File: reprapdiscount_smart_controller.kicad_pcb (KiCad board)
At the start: 2 copper layers, 150 x 55 mm, 17 parts, among them Q1 BC817, U1 74HC4050, U2 MIC5209

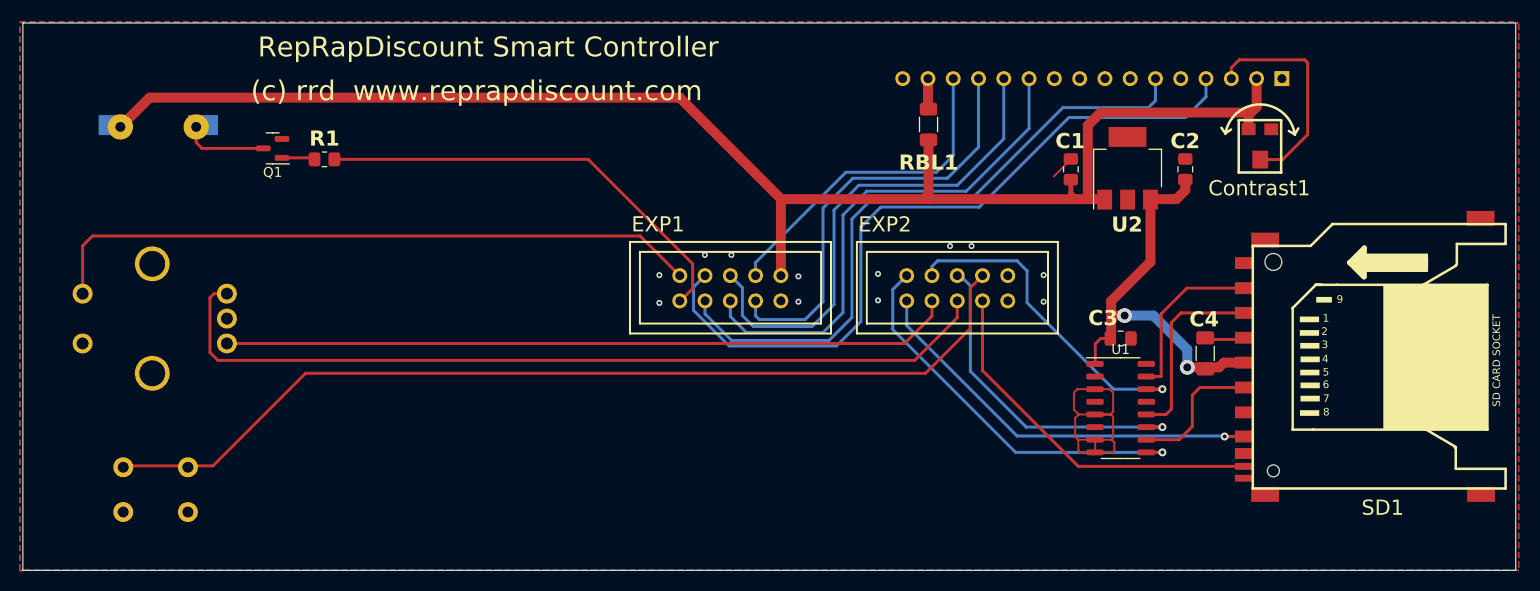
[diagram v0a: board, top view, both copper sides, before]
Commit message: fixup: restore mounting holes lost during cleanup
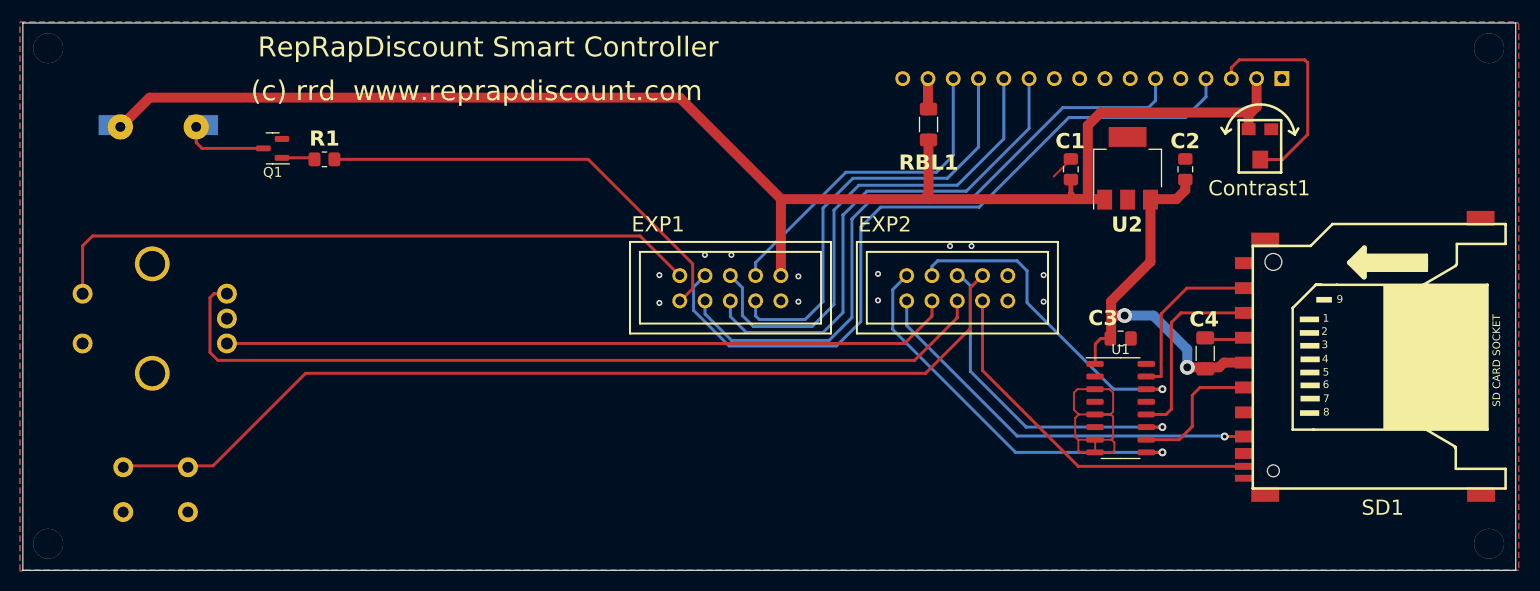
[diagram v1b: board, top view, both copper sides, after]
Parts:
- added H1: MountingHole, reprapdiscount_smart_controller:MountingHole_3mm, F.Cu at (76.0, 80.0)
- added H2: MountingHole, reprapdiscount_smart_controller:MountingHole_3mm, F.Cu at (220.8, 80.0)
- added H3: MountingHole, reprapdiscount_smart_controller:MountingHole_3mm, F.Cu at (76.0, 129.8)
- added H4: MountingHole, reprapdiscount_smart_controller:MountingHole_3mm, F.Cu at (220.8, 129.8)

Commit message: fixup: fix reset button height
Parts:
- PB1: footprint Button_Switch_THT:SW_PUSH_6mm_H5mm -> Button_Switch_THT:SW_PUSH_6mm_H7.3mm
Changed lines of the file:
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@@
     )
   )
-  (footprint "Button_Switch_THT:SW_PUSH_6mm_H5mm" locked (layer "B.Cu")
+  (footprint "Button_Switch_THT:SW_PUSH_6mm_H7.3mm" locked (layer "B.Cu")
     (at 90.0841 122.1436 180)
-    (descr "tactile push button, 6x6mm e.g. PHAP33xx series, height=5mm")
+    (descr "tactile push button, 6x6mm e.g. PHAP33xx series, height=7.3mm")
     (tags "tact sw push 6mm")
     (property "Sheetfile" "reprapdiscount_smart_controller.kicad_sch")
@@
     (property "ki_keywords" "switch normally-open pushbutton push-button")
     (attr through_hole)
-    (fp_text reference "PB1" (at 3.25 2.286) (layer "B.SilkS")
-        (effects (font (size 1.524 1.524) (thickness 0.254) bold) (justify mirror))
+    (fp_text reference "PB1" (at 3.25 2) (layer "B.SilkS")
+        (effects (font (size 1 1) (thickness 0.15)) (justify mirror))
     )
-    (fp_text value "STOP" (at 3.75 -6.985) (layer "B.SilkS")
-        (effects (font (size 1.524 1.524) (thickness 0.254) bold) (justify mirror))
+    (fp_text value "STOP" (at 3.75 -6.7) (layer "B.Fab")
+        (effects (font (size 1 1) (thickness 0.15)) (justify mirror))
     )
     (fp_text user "${REFERENCE}" (at 3.25 -2.25) (layer "B.Fab")
@@
     (pad "2" thru_hole circle locked (at 6.5 -4.5 90) (size 2 2) (drill 1.1) (layers "*.Cu" "*.Mask")
       (net 6 "GND") (pinfunction "2") (pintype "passive"))
-    (model "${KICAD6_3DMODEL_DIR}/Button_Switch_THT.3dshapes/SW_PUSH_6mm_H5mm.wrl"
+    (model "${KICAD6_3DMODEL_DIR}/Button_Switch_THT.3dshapes/SW_PUSH_6mm_H7.3mm.wrl"
       (offset (xyz 0 0 0))
       (scale (xyz 1 1 1))

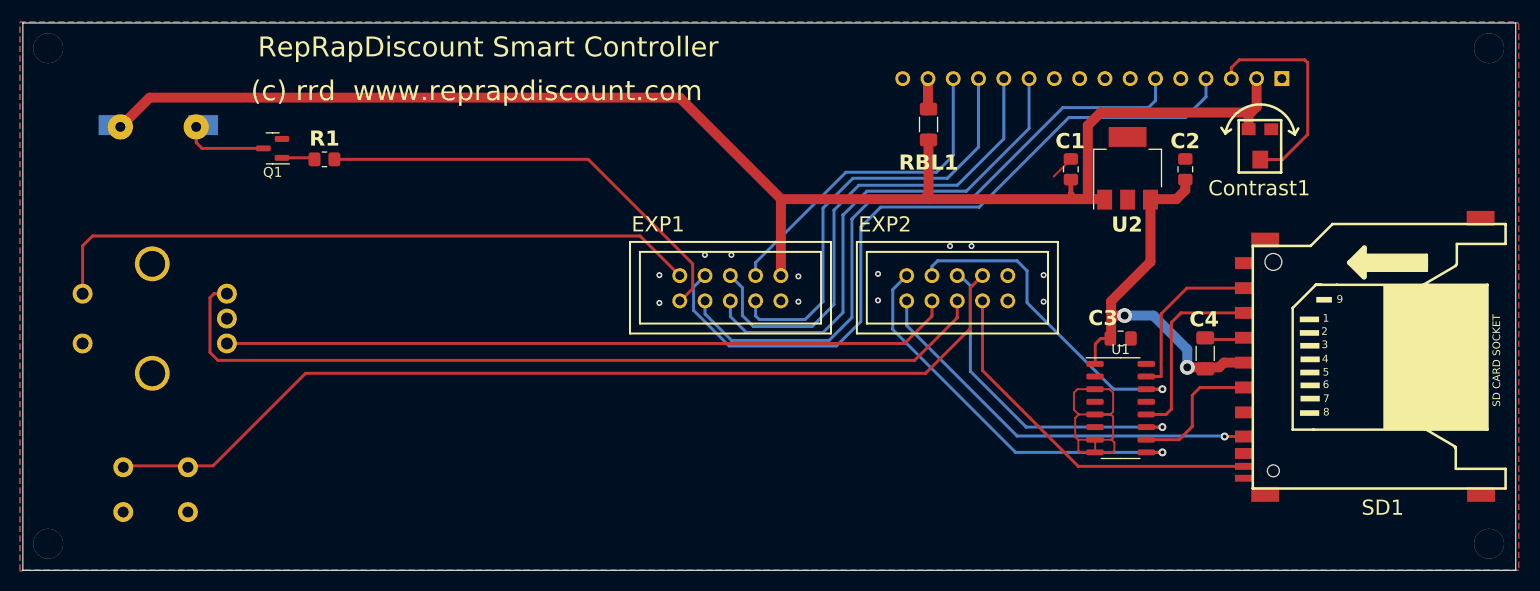
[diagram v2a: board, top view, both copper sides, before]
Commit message: feature: add parts from ldo-rrlcd-a007
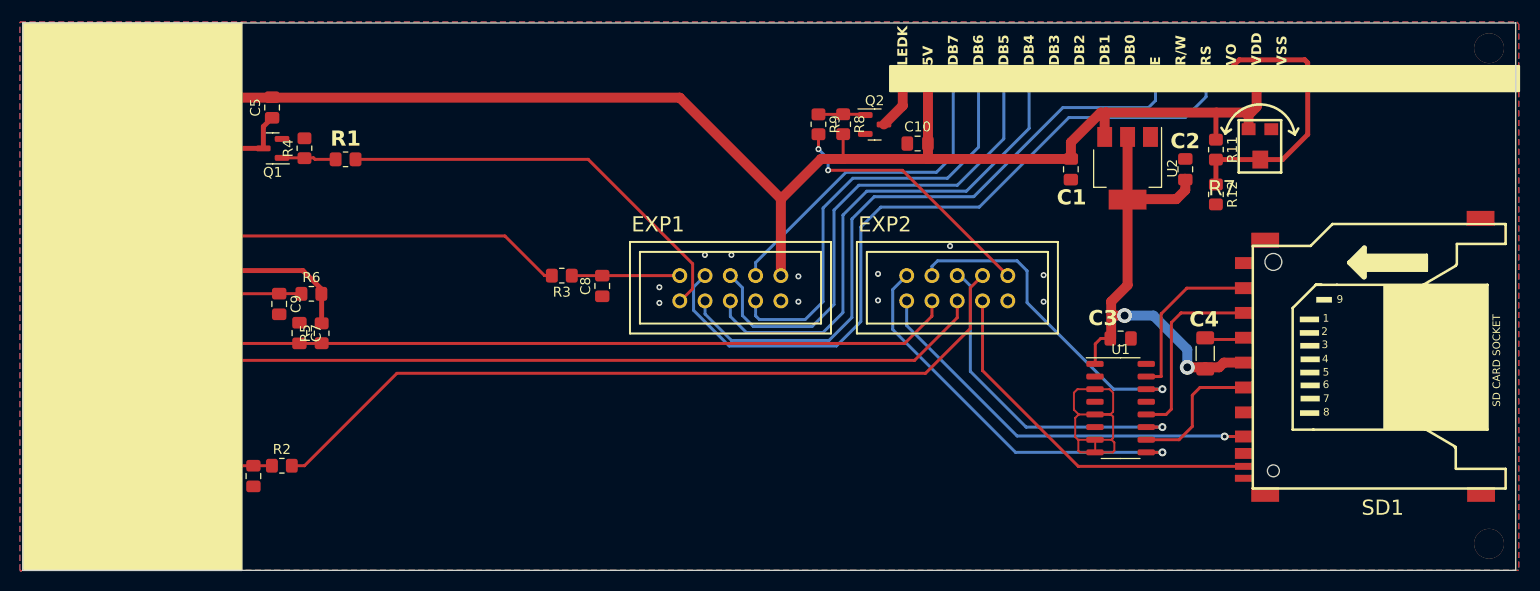
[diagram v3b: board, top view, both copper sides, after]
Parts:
- removed RBL1: 68, Resistor_SMD:R_1206_3216Metric_Pad1.30x1.75mm_HandSolder
- added C10: 10u, Capacitor_SMD:C_0805_2012Metric_Pad1.18x1.45mm_HandSolder, F.Cu at (163.4, 89.6)
- added C5: 100n, Capacitor_SMD:C_0805_2012Metric_Pad1.18x1.45mm_HandSolder, F.Cu at (98.5, 86.0)
- added C6: 100n, Capacitor_SMD:C_0805_2012Metric_Pad1.18x1.45mm_HandSolder, F.Cu at (96.7, 123.0)
- added C7: 100n, Capacitor_SMD:C_0805_2012Metric_Pad1.18x1.45mm_HandSolder, F.Cu at (101.3, 108.7)
- added C8: 100n, Capacitor_SMD:C_0805_2012Metric_Pad1.18x1.45mm_HandSolder, F.Cu at (131.7, 103.9)
- added C9: 100n, Capacitor_SMD:C_0805_2012Metric_Pad1.18x1.45mm_HandSolder, F.Cu at (99.3, 105.7)
- added Q2: BC817, Package_TO_SOT_SMD:SOT-23, F.Cu at (159.1, 87.7)
- added R11: DNI, Resistor_SMD:R_0805_2012Metric_Pad1.20x1.40mm_HandSolder, F.Cu at (193.4, 90.2)
- added R12: 470R, Resistor_SMD:R_0805_2012Metric_Pad1.20x1.40mm_HandSolder, F.Cu at (193.4, 94.7)
- added R2: 1k, Resistor_SMD:R_0805_2012Metric_Pad1.20x1.40mm_HandSolder, F.Cu at (99.5, 122.0)
- added R3: 100R, Resistor_SMD:R_0805_2012Metric_Pad1.20x1.40mm_HandSolder, F.Cu at (127.7, 102.9)
- added R4: 5.1k, Resistor_SMD:R_0805_2012Metric_Pad1.20x1.40mm_HandSolder, F.Cu at (101.8, 90.1)
- added R5: 5.1k, Resistor_SMD:R_0805_2012Metric_Pad1.20x1.40mm_HandSolder, F.Cu at (103.5, 108.7)
- added R6: 5.1k, Resistor_SMD:R_0805_2012Metric_Pad1.20x1.40mm_HandSolder, F.Cu at (102.5, 104.7)
- added R8: 10k, Resistor_SMD:R_0805_2012Metric_Pad1.20x1.40mm_HandSolder, F.Cu at (155.9, 87.7)
- added R9: 100R, Resistor_SMD:R_0805_2012Metric_Pad1.20x1.40mm_HandSolder, F.Cu at (153.4, 87.7)
- C1, C2: value 100nF -> 10u
- C3: value 100nF -> 100n
- C4: value 1uF -> 10u
- R7: renamed from Contrast1; value 10K -> 1.4k
- U2: value MIC5209 -> AMS1117-3.3; footprint Package_TO_SOT_SMD:SOT-223 -> Package_TO_SOT_SMD:SOT-223-3_TabPin2
- moved R1 2.12 mm to (105.9, 91.2)
- turned C1 to 90 degrees
- turned U2 to -90 degrees
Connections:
- EN1 pad 5: BTN_ENC -> Net-(EN1-Pad5)
- EXP2 pad 10: /KILL -> PWR_LED
- LCD1 pad 15: Net-(LCD1-A+) -> VCC
- LCD1 pad 16: GND -> LEDK
- PB1 pad 1: /RESET -> Net-(C6-Pad2)
- U2 pad 1: VCC -> GND
- U2 pad 2: GND -> +3V3
- U2 pad 3: +3V3 -> VCC
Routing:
- net BTN_ENC: track 66.9 -> 10.9 mm
- net VCC: track 150.3 -> 205.1 mm
- net Net-(EN1-Pad5): track 0.00 -> 51.2 mm
- net PWR_LED: track 0.00 -> 26.5 mm, vias 0 -> 2
- net /RESET: track 96.8 -> 79.7 mm
- net Net-(C6-Pad2): track 0.00 -> 17.0 mm
- net +3V3: track 41.2 -> 48.8 mm
- net BTN_EN1: track 86.2 -> 93.7 mm
- net Net-(LCD1-Vo): track 22.2 -> 29.2 mm
- net LEDK: track 0.00 -> 5.39 mm
- net Net-(Q2-B): track 0.00 -> 4.74 mm
- net Net-(PZ1-+): track 8.50 -> 11.9 mm
- net Net-(LCD1-A+): track 3.27 -> 0.00 mm
- net GND: track 36.3 -> 33.9 mm, vias 12 -> 11
- net BEEPER: track 44.6 -> 42.5 mm
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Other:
- board text added: "5V"
- board text added: "DB0"
- board text added: "DB1"
- board text added: "DB2"
- board text added: "DB3"
- board text added: "DB4"
- board text added: "DB5"
- board text added: "DB6"
- board text added: "DB7"
- board text added: "E"
- board text added: "LEDK"
- board text added: "R/W"
- board text added: "RS"
- board text added: "VO"
- board text added: "VSS"
- board text removed: "(c) rrd www.reprapdiscount.com"
- board text removed: "RepRapDiscount Smart Controller"

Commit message: feature: add fiducials
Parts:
- added FID1: Fiducial, Fiducial:Fiducial_1mm_Mask2mm, F.Cu at (103.5, 81.5)
- added FID2: Fiducial, Fiducial:Fiducial_1mm_Mask2mm, F.Cu at (213.5, 128.5)
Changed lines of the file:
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@@
     )
+  )
+  (footprint "Fiducial:Fiducial_1mm_Mask2mm" (layer "F.Cu")
+    (at 213.5011 128.5036)
+    (descr "Circular Fiducial, 1mm bare copper, 2mm soldermask opening (Level A)")
+    (tags "fiducial")
+    (property "Sheetfile" "reprapdiscount_smart_controller.kicad_sch")
+    (property "Sheetname" "")
+    (property "ki_description" "Fiducial Marker")
+    (property "ki_keywords" "fiducial marker")
+    (attr smd)
+    (fp_text reference "FID2" (at 0 -2) (layer "F.Fab")
+        (effects (font (size 1 1) (thickness 0.15)))
+    )
+    (fp_text value "Fiducial" (at 0 2) (layer "F.Fab")
+        (effects (font (size 1 1) (thickness 0.15)))
+    )
+    (fp_text user "${REFERENCE}" (at 0 0) (layer "F.Fab")
+        (effects (font (size 0.4 0.4) (thickness 0.06)))
+    )
+    (fp_circle (center 0 0) (end 1.25 0)
+      (stroke (width 0.05) (type solid)) (fill none) (layer "F.CrtYd"))
+    (fp_circle (center 0 0) (end 1 0)
+      (stroke (width 0.1) (type solid)) (fill none) (layer "F.Fab"))
+    (pad "" smd circle (at 0 0) (size 1 1) (layers "F.Cu" "F.Mask")
+      (solder_mask_margin 0.5) (clearance 0.5))
   )
   (footprint "Resistor_SMD:R_0805_2012Metric_Pad1.20x1.40mm_HandSolder" (layer "F.Cu")
@@
     )
   )
+  (footprint "Fiducial:Fiducial_1mm_Mask2mm" (layer "F.Cu")
+    (at 103.5011 81.5036)
+    (descr "Circular Fiducial, 1mm bare copper, 2mm soldermask opening (Level A)")
+    (tags "fiducial")
+    (property "Sheetfile" "reprapdiscount_smart_controller.kicad_sch")
+    (property "Sheetname" "")
+    (property "ki_description" "Fiducial Marker")
+    (property "ki_keywords" "fiducial marker")
+    (attr smd)
+    (fp_text reference "FID1" (at 0 -2) (layer "F.Fab")
+        (effects (font (size 1 1) (thickness 0.15)))
+    )
+    (fp_text value "Fiducial" (at 0 2) (layer "F.Fab")
+        (effects (font (size 1 1) (thickness 0.15)))
+    )
+    (fp_text user "${REFERENCE}" (at 0 0) (layer "F.Fab")
+        (effects (font (size 0.4 0.4) (thickness 0.06)))
+    )
+    (fp_circle (center 0 0) (end 1.25 0)
+      (stroke (width 0.05) (type solid)) (fill none) (layer "F.CrtYd"))
+    (fp_circle (center 0 0) (end 1 0)
+      (stroke (width 0.1) (type solid)) (fill none) (layer "F.Fab"))
+    (pad "" smd circle (at 0 0) (size 1 1) (layers "F.Cu" "F.Mask")
+      (solder_mask_margin 0.5) (clearance 0.5))
+  )
   (footprint "Button_Switch_THT:SW_PUSH_6mm_H7.3mm" locked (layer "B.Cu")

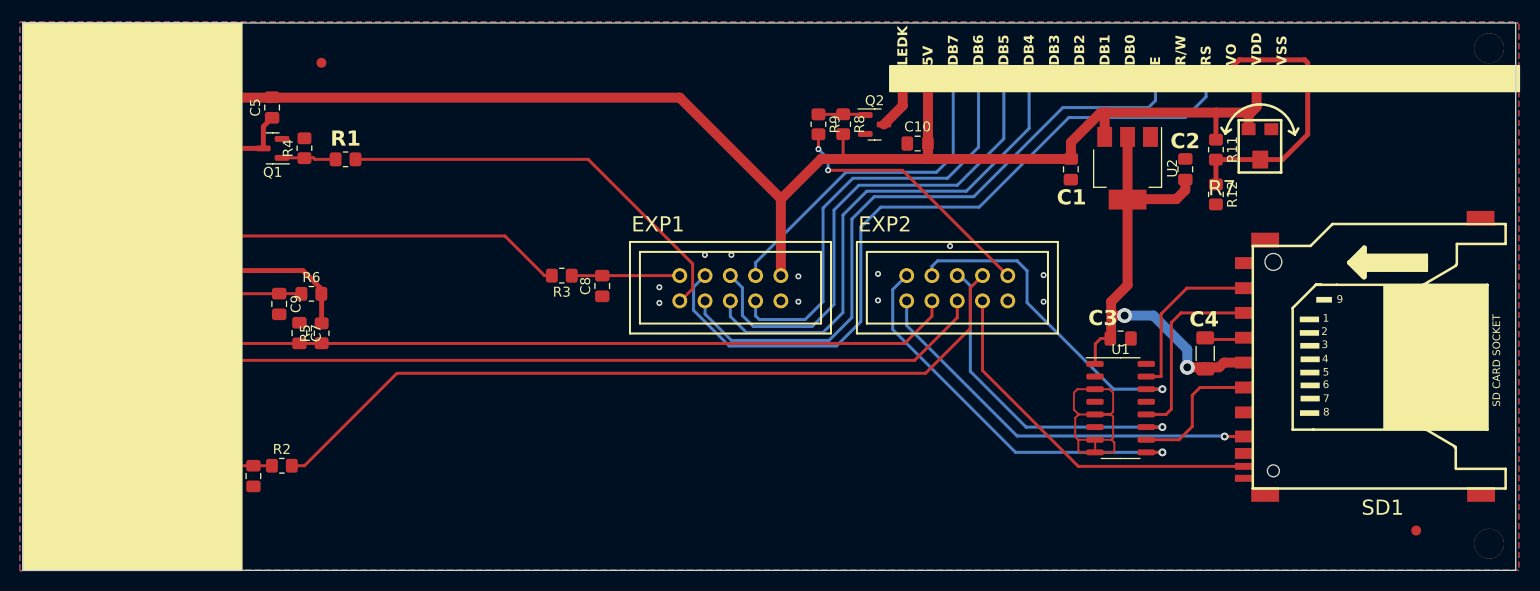
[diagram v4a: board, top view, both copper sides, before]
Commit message: silkscreen: update to match ldo-rrlcd-a007
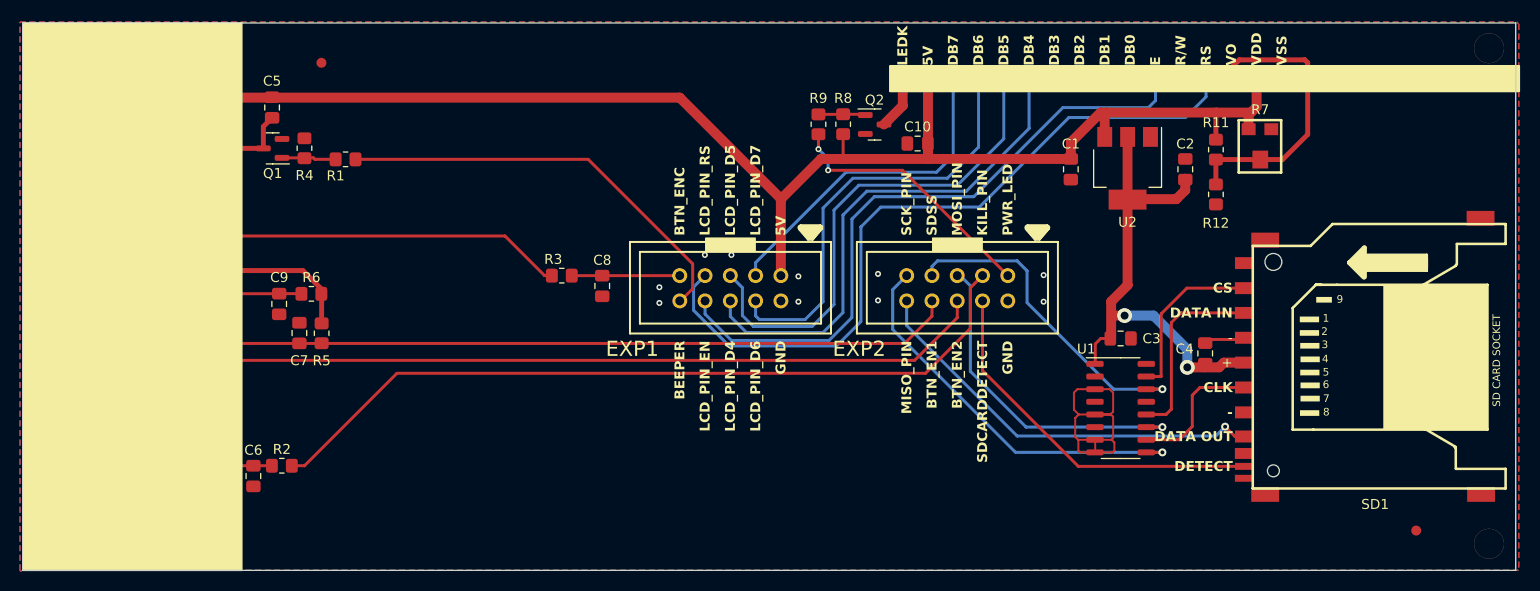
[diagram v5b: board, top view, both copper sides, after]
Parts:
- C4: footprint Capacitor_SMD:C_1206_3216Metric_Pad1.33x1.80mm_HandSolder -> Capacitor_SMD:C_0805_2012Metric_Pad1.18x1.45mm_HandSolder
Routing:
- net /PB3_(MISO): track 41.2 -> 41.8 mm
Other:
- board text added: "+"
- board text added: "-"
- board text added: "BEEPER"
- board text added: "BTN_EN1"
- board text added: "BTN_EN2"
- board text added: "BTN_ENC"
- board text added: "DATA IN"
- board text added: "DATA OUT"
- board text added: "DETECT"
- board text added: "GND"
- board text added: "KILL_PIN"
- board text added: "Kill"
- board text added: "LCD_PIN_D4"
- board text added: "LCD_PIN_D5"
- board text added: "LCD_PIN_D6"
- board text added: "LCD_PIN_D7"
- board text added: "LCD_PIN_EN"
- board text added: "LCD_PIN_RS"
- board text added: "MISO_PIN"
- board text added: "MOSI_PIN"
- board text added: "PWR_LED"
- board text added: "SCK_PIN"
- board text added: "SDCARDDETECT"
- board text added: "SDSS"
